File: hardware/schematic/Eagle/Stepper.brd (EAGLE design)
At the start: 42.8 x 43.2 mm, 36 parts, among them U16 MMSZ5225BT1G, U19 LM358DR

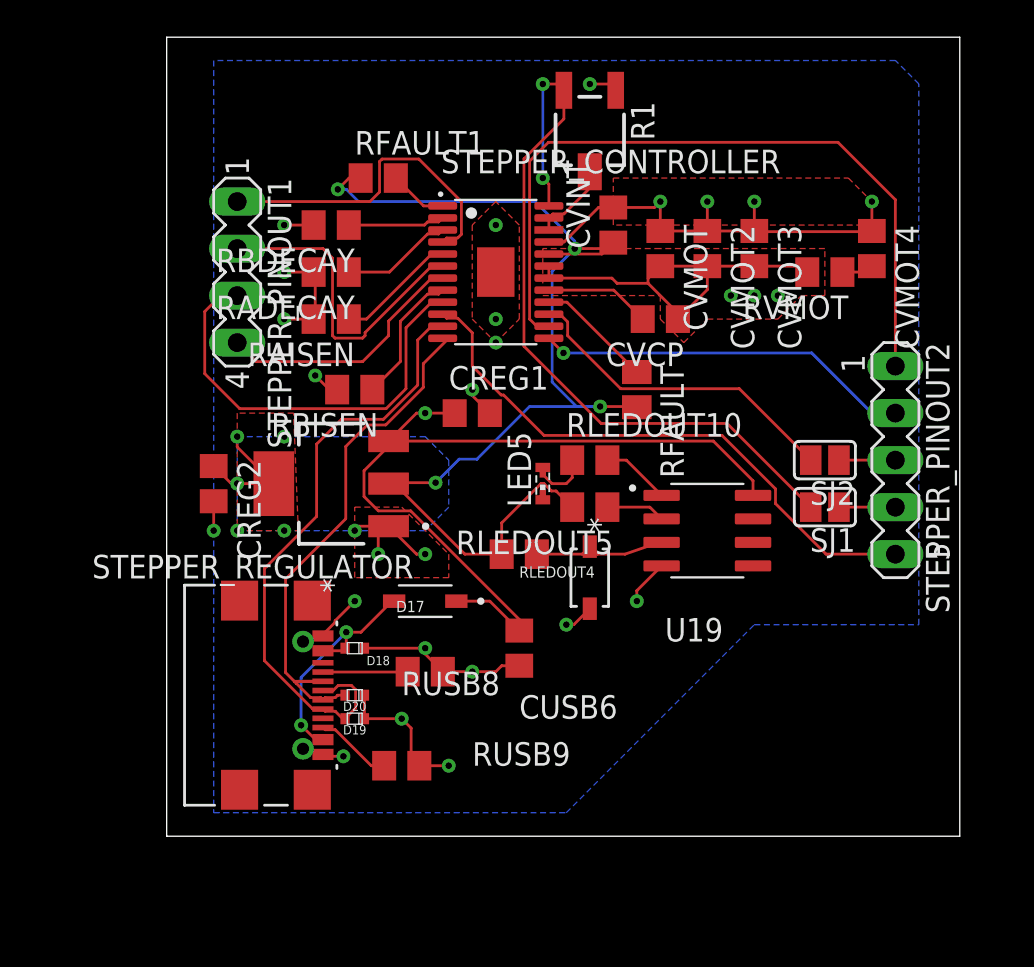
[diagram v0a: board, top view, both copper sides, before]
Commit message: Added Silkscreen text, widened approiate traces, added mounting holes
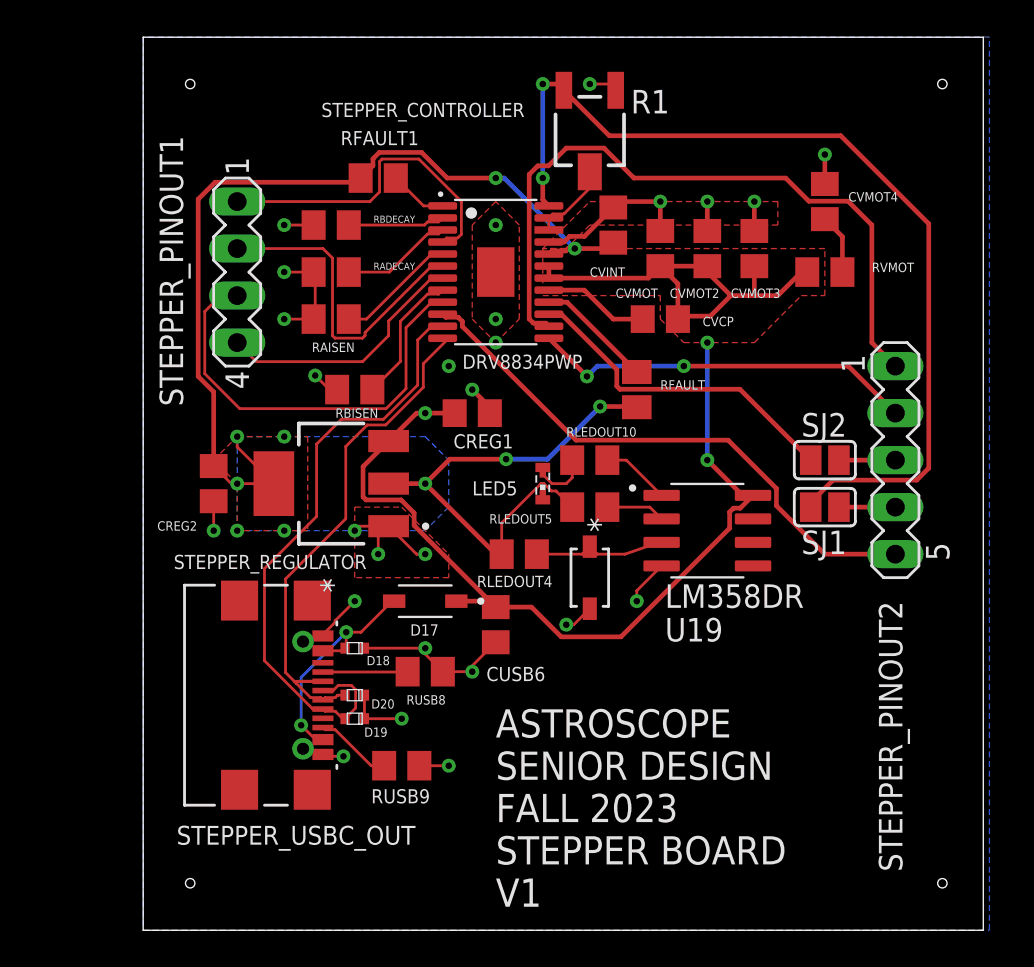
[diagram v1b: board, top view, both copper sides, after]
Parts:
- moved CVMOT4 3.59 mm to (67.3, 48.3)
- moved CUSB6 1.80 mm to (49.5, 25.4)
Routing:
- net GND: track 69.5 -> 54.6 mm
- net VREF: track 41.8 -> 51.3 mm
- net 3.3VOUTUSB2: track 73.0 -> 80.6 mm, vias 9 -> 10
- net 5VOUTUSB2: track 66.3 -> 72.9 mm, vias 4 -> 3
- net N$37: track 40.2 -> 38.0 mm
- net N$20: track 1.72 -> 3.25 mm
- net N$90: track 31.4 -> 30.5 mm
- net N$38: track 20.4 -> 20.9 mm, vias 1 -> 2
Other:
- board size 42.8 x 43.2 mm -> 45.4 x 48.2 mm
- board text added: "ASTROSCOPE SENIOR DESIGN FALL 2023 STEPPER BOARD V1"

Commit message: updated with Dr.Week's advice
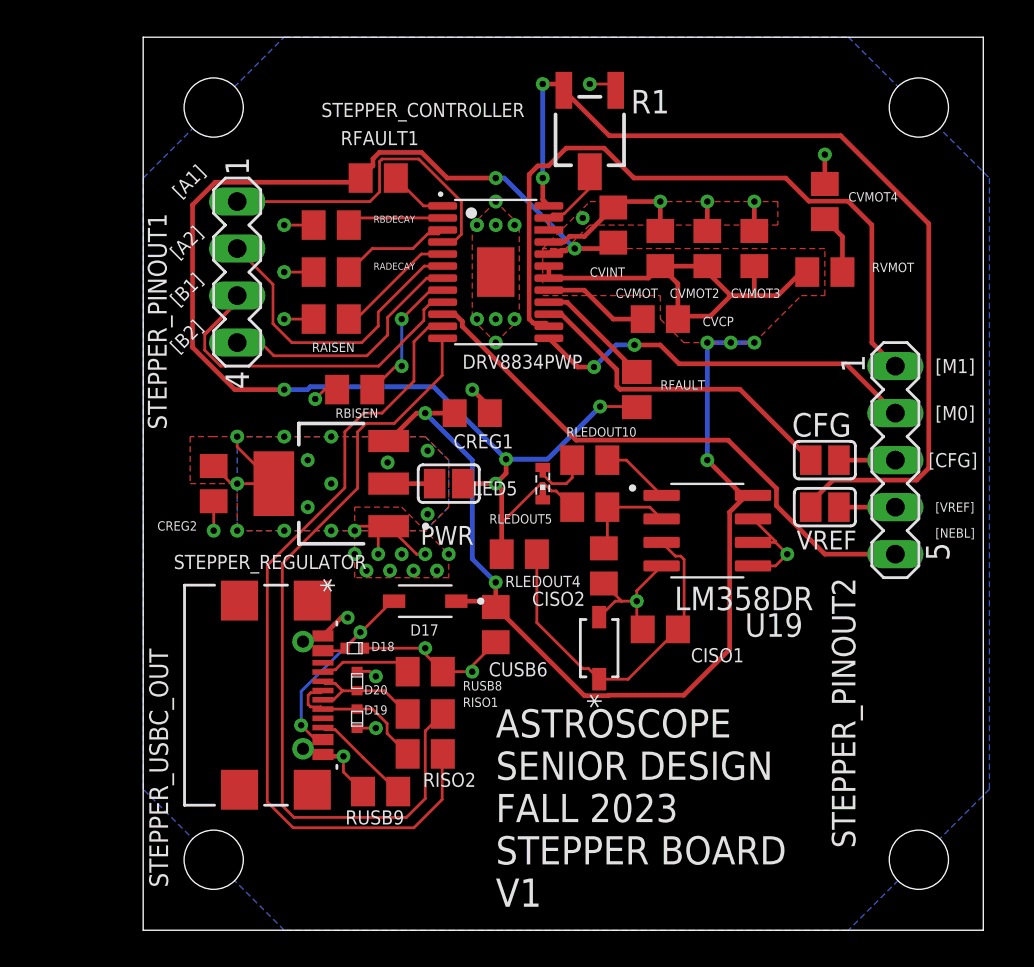
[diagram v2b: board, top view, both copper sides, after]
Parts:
- added CISO1, CISO2: 0.01uF, rcl:C0805
- added PWR: (no value), jumper:SJ
- added RISO1, RISO2: 1.5k, rcl:M0805
- moved U16 3.84 mm to (55.1, 24.1), turned to 90 degrees
- moved RUSB9 1.81 mm to (43.3, 16.4), turned to 180 degrees
- moved D20 0.77 mm to (42.0, 22.4), turned to 270 degrees
- moved D19 0.13 mm to (42.0, 20.3), turned to 90 degrees
- renumbered SJ1 to VREF, SJ2 to CFG
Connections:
- net N$28 renamed AOUT1
- net N$29 renamed AOUT2
- net N$30 renamed BOUT1
- net N$31 renamed BOUT2
- net N$34 renamed VREFOUT
- net N$35 renamed CONFIGOUT
- net N$37 renamed M1OUT
- net N$38 renamed M0OUT
- net N$90 renamed NENBL
- removed net N$87: U19.6
- removed net N$89: U19.5
- new net 3.3VREGOUT: CREG2.1, PWR.1, STEPPER_REGULATOR.2, STEPPER_REGULATOR.4
- new net N$1: RISO1.1, STEPPER_CONTROLLER.12
- new net N$2: RISO2.1, STEPPER_CONTROLLER.11
- net 3.3VOUTUSB2: now also PWR.2; no longer CREG2.1, STEPPER_REGULATOR.2, STEPPER_REGULATOR.4
- net GND: now also CISO1.2, CISO2.2, U19.5, U19.6, U19.7
- net GPIO8M: now also RISO2.2; no longer STEPPER_CONTROLLER.11
- net GPIO9M: now also RISO1.2; no longer STEPPER_CONTROLLER.12
- net N$82: now also CISO1.1
- net N$83: now also CISO2.1
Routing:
- net N$2: track 0.00 -> 43.8 mm
- net N$1: track 0.00 -> 43.1 mm, vias 1 -> 0
- net GPIO8M: track 33.2 -> 8.20 mm
- net GPIO9M: track 29.6 -> 6.57 mm
- net 3.3VREGOUT: track 0.00 -> 12.6 mm, vias 0 -> 13
- net N$82: track 7.18 -> 19.2 mm
- net 5VOUTUSB2: track 72.9 -> 80.0 mm, vias 3 -> 6
- net GND: track 54.6 -> 61.4 mm, vias 25 -> 38
- net BOUT1: track 23.4 -> 18.7 mm
- net 3.3VOUTUSB2: track 80.6 -> 78.1 mm, vias 10 -> 6
- net N$83: track 3.19 -> 5.50 mm
- net N$73: track 4.16 -> 5.48 mm
- net AOUT2: track 17.3 -> 16.6 mm
- net M0OUT: track 20.9 -> 21.4 mm
- net N$21: track 7.30 -> 7.51 mm, vias 0 -> 2
- added copper zone on layer 1, net 3.3VREGOUT
- added copper zone on layer 16, net 3.3VREGOUT
- removed copper zone on layer 1, net 3.3VOUTUSB2
- removed copper zone on layer 16, net 3.3VOUTUSB2
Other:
- board text added: "[A1]"
- board text added: "[A2]"
- board text added: "[B1]"
- board text added: "[B2]"
- board text added: "[CFG]"
- board text added: "[M0]"
- board text added: "[M1]"
- board text added: "[NEBL]"
- board text added: "[VREF]"
